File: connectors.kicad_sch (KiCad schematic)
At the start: 13 parts, among them J1 USB-C_JAE_DX07S024JJ2, J2 PCIe_x4_Conn_EdgeMount_Open, J3 Molex_Nano-Fit_1x2_1053131102

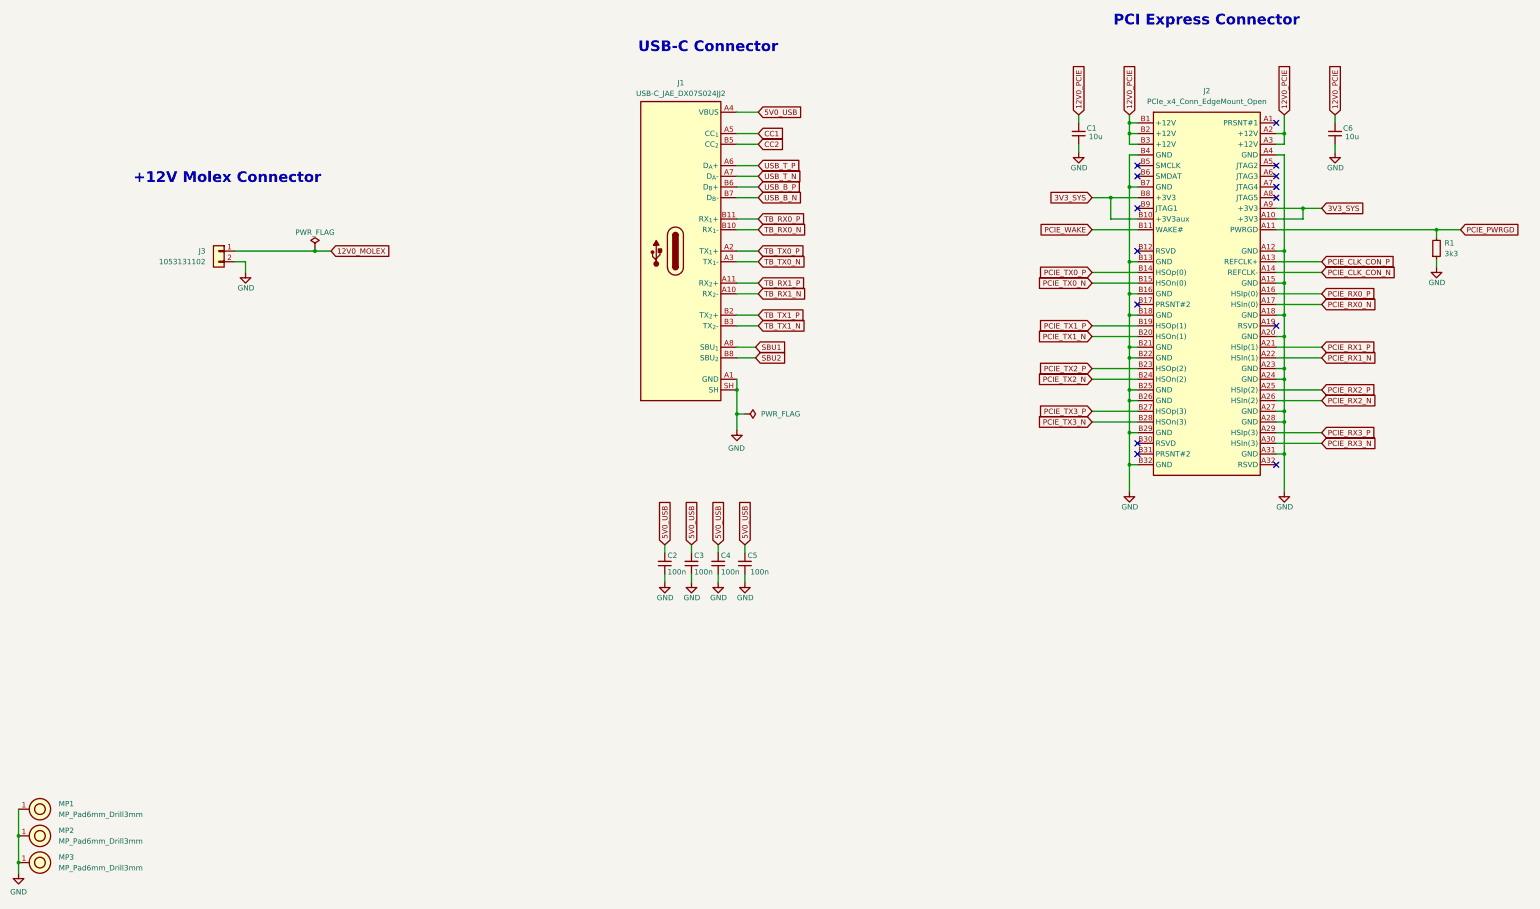
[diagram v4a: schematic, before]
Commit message: [#58582] Update symbols values visibility
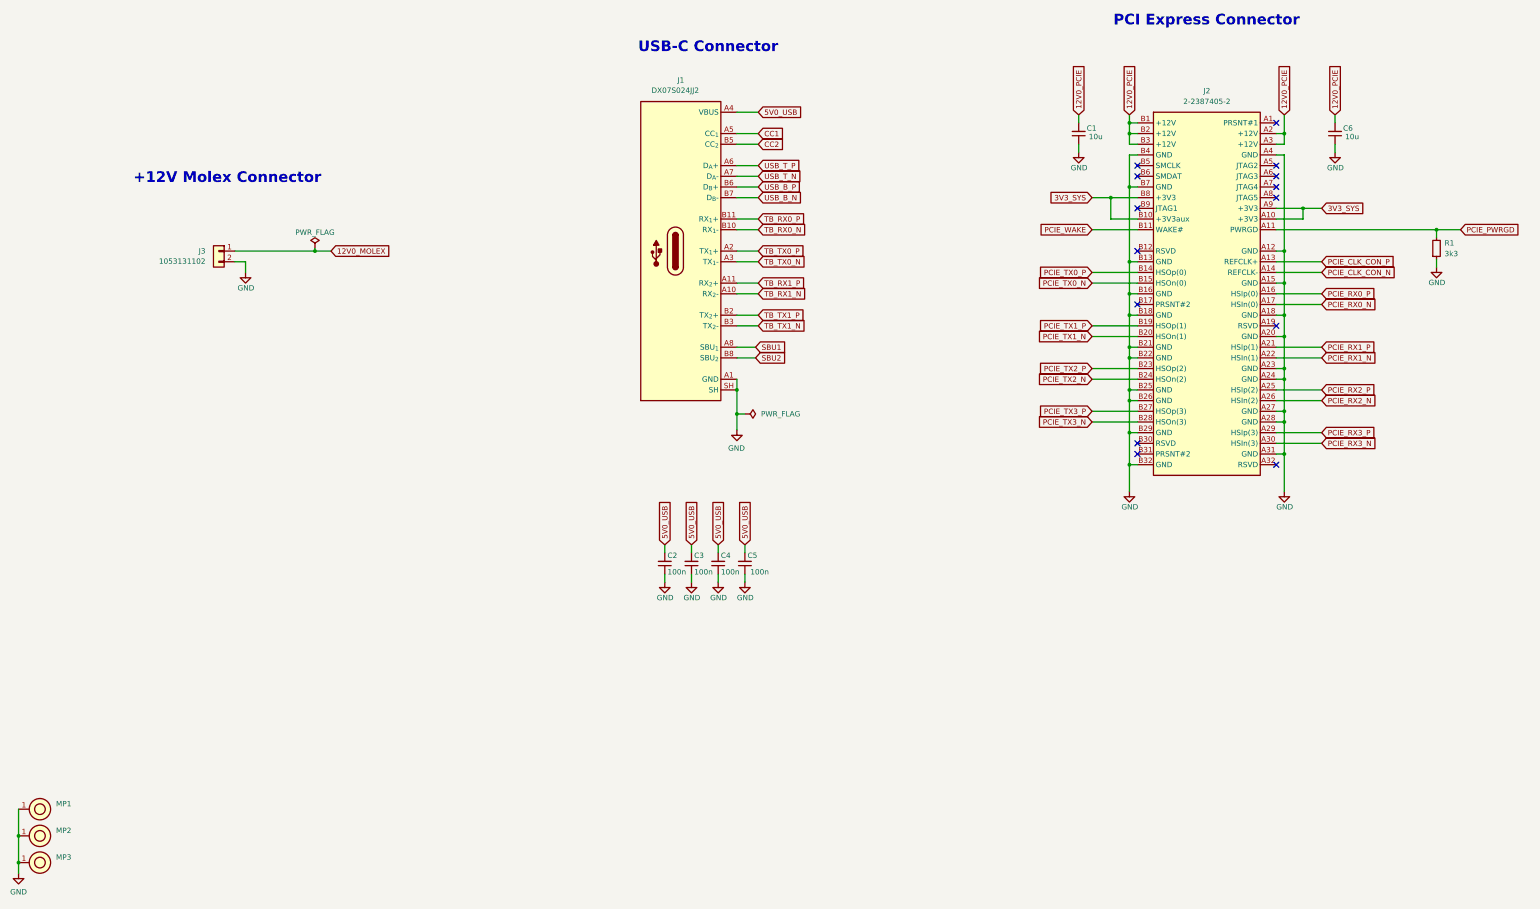
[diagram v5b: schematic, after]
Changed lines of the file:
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@@
   (symbol (lib_id "antmicroMechanicalParts:MP_Pad6mm_Drill3mm") (at 30.48 263.525 0) (unit 1)
     (in_bom no) (on_board yes) (dnp no) (fields_autoplaced)
-    (property "Reference" "MP1" (at 40.005 262.255 0)
+    (property "Reference" "MP1" (at 39.37 262.255 0)
       (effects (font (size 1.27 1.27) (thickness 0.15)) (justify left))
     )
-    (property "Value" "MP_Pad6mm_Drill3mm" (at 40.005 264.795 0)
-      (effects (font (size 1.27 1.27) (thickness 0.15)) (justify left))
+    (property "Value" "MP_Pad6mm_Drill3mm" (at 39.37 264.795 0)
+      (effects (font (size 1.27 1.27) (thickness 0.15)) (justify left) hide)
     )
     (property "Footprint" "antmicro-footprints:MP_Pad6mm_Drill3mm" (at 50.8 271.145 0)
@@
       (effects (font (size 1.27 1.27) (thickness 0.15)) (justify left bottom) hide)
     )
-    (property "MPN" "1053131102" (at 74.93 133.35 0)
-      (effects (font (size 1.27 1.27) (thickness 0.15)) (justify left))
+    (property "MPN" "1053131102" (at 74.93 133.985 0)
+      (effects (font (size 1.27 1.27) (thickness 0.15)) (justify left bottom))
     )
     (property "Author" "Antmicro" (at 68.58 148.59 0)
@@
     )
   )
-  (symbol (lib_name "USB-C_JAE_DX07S024JJ2_1") (lib_id "antmicroUSBConnectors:USB-C_JAE_DX07S024JJ2") (at 201.295 97.79 0) (unit 1)
-    (in_bom yes) (on_board yes) (dnp no) (fields_autoplaced)
-    (property "Reference" "J1" (at 187.96 90.805 0)
+  (symbol (lib_id "antmicroUSBConnectors:USB-C_JAE_DX07S024JJ2") (at 201.295 97.79 0) (unit 1)
+    (in_bom yes) (on_board yes) (dnp no)
+    (property "Reference" "J1" (at 187.96 90.17 0)
       (effects (font (size 1.27 1.27) (thickness 0.15)))
     )
-    (property "Value" "USB-C_JAE_DX07S024JJ2" (at 187.96 93.345 0)
-      (effects (font (size 1.27 1.27) (thickness 0.15)))
+    (property "Value" "USB-C_JAE_DX07S024JJ2" (at 187.96 92.71 0)
+      (effects (font (size 1.27 1.27) (thickness 0.15)) hide)
     )
     (property "Footprint" "antmicro-footprints:USB-C_Receptacle_JAE_DX07S024JJ2" (at 238.125 100.33 0)
@@
       (effects (font (size 1.27 1.27) (thickness 0.15)) (justify left bottom) hide)
     )
-    (property "MPN" "DX07S024JJ2" (at 238.125 105.41 0)
-      (effects (font (size 1.27 1.27) (thickness 0.15)) (justify left bottom) hide)
+    (property "MPN" "DX07S024JJ2" (at 180.975 93.345 0)
+      (effects (font (size 1.27 1.27) (thickness 0.15)) (justify left bottom))
     )
     (property "Manufacturer" "JAE Electronics" (at 238.125 107.95 0)
@@
   (symbol (lib_id "antmicroMechanicalParts:MP_Pad6mm_Drill3mm") (at 30.48 269.875 0) (unit 1)
     (in_bom no) (on_board yes) (dnp no) (fields_autoplaced)
-    (property "Reference" "MP2" (at 40.005 268.605 0)
+    (property "Reference" "MP2" (at 39.37 268.605 0)
       (effects (font (size 1.27 1.27) (thickness 0.15)) (justify left))
     )
-    (property "Value" "MP_Pad6mm_Drill3mm" (at 40.005 271.145 0)
-      (effects (font (size 1.27 1.27) (thickness 0.15)) (justify left))
+    (property "Value" "MP_Pad6mm_Drill3mm" (at 39.37 271.145 0)
+      (effects (font (size 1.27 1.27) (thickness 0.15)) (justify left) hide)
     )
     (property "Footprint" "antmicro-footprints:MP_Pad6mm_Drill3mm" (at 50.8 277.495 0)
@@
       (effects (font (size 1.27 1.27) (thickness 0.15)))
     )
-    (property "Value" "PCIe_x4_Conn_EdgeMount_Open" (at 313.055 95.25 0)
+    (property "Value" "PCIe_x4_Conn_EdgeMount_Open" (at 344.805 105.41 0)
+      (effects (font (size 1.27 1.27) (thickness 0.15)) (justify left bottom) hide)
+    )
+    (property "Footprint" "antmicro-footprints:PCIE_TE_2-2387405-2" (at 344.805 107.95 0)
+      (effects (font (size 1.27 1.27) (thickness 0.15)) (justify left bottom) hide)
+    )
+    (property "Datasheet" "https://www.te.com/commerce/DocumentDelivery/DDEController?Action=showdoc&DocId=Customer+Drawing%7F2387405%7FA%7Fpdf%7FEnglish%7FENG_CD_2387405_A.pdf%7F2-2387405-2" (at 344.805 110.49 0)
+      (effects (font (size 1.27 1.27) (thickness 0.15)) (justify left bottom) hide)
+    )
+    (property "MPN" "2-2387405-2" (at 313.055 95.25 0)
       (effects (font (size 1.27 1.27) (thickness 0.15)))
-    )
-    (property "Footprint" "antmicro-footprints:PCIE_TE_2-2387405-2" (at 344.805 107.95 0)
-      (effects (font (size 1.27 1.27) (thickness 0.15)) (justify left bottom) hide)
-    )
-    (property "Datasheet" "https://www.te.com/commerce/DocumentDelivery/DDEController?Action=showdoc&DocId=Customer+Drawing%7F2387405%7FA%7Fpdf%7FEnglish%7FENG_CD_2387405_A.pdf%7F2-2387405-2" (at 344.805 110.49 0)
-      (effects (font (size 1.27 1.27) (thickness 0.15)) (justify left bottom) hide)
-    )
-    (property "MPN" "2-2387405-2" (at 344.805 113.03 0)
-      (effects (font (size 1.27 1.27) (thickness 0.15)) (justify left bottom) hide)
     )
     (property "Manufacturer" "TE Connectivity" (at 344.805 115.57 0)
@@
   (symbol (lib_id "antmicroMechanicalParts:MP_Pad6mm_Drill3mm") (at 30.48 276.225 0) (unit 1)
     (in_bom no) (on_board yes) (dnp no) (fields_autoplaced)
-    (property "Reference" "MP3" (at 40.005 274.955 0)
+    (property "Reference" "MP3" (at 39.37 274.955 0)
       (effects (font (size 1.27 1.27) (thickness 0.15)) (justify left))
     )
-    (property "Value" "MP_Pad6mm_Drill3mm" (at 40.005 277.495 0)
-      (effects (font (size 1.27 1.27) (thickness 0.15)) (justify left))
+    (property "Value" "MP_Pad6mm_Drill3mm" (at 39.37 277.495 0)
+      (effects (font (size 1.27 1.27) (thickness 0.15)) (justify left) hide)
     )
     (property "Footprint" "antmicro-footprints:MP_Pad6mm_Drill3mm" (at 50.8 283.845 0)

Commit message: [#58582] Update J3, L3 symbols and footprints
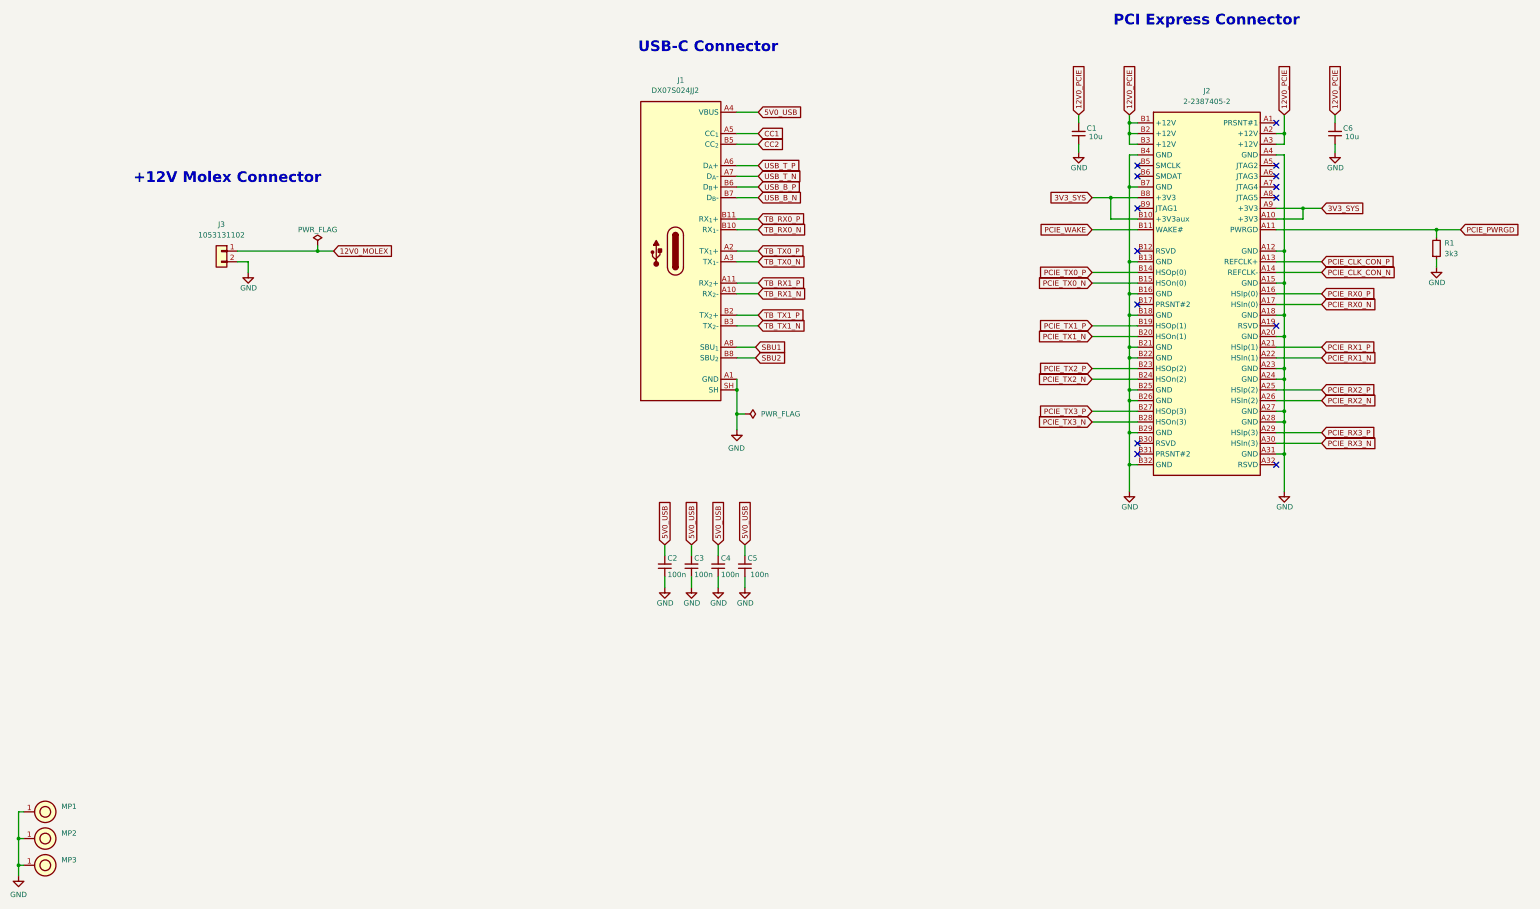
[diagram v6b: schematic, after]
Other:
- moved on the sheet: C2, C3, C4, C5, MP1, MP2, MP3

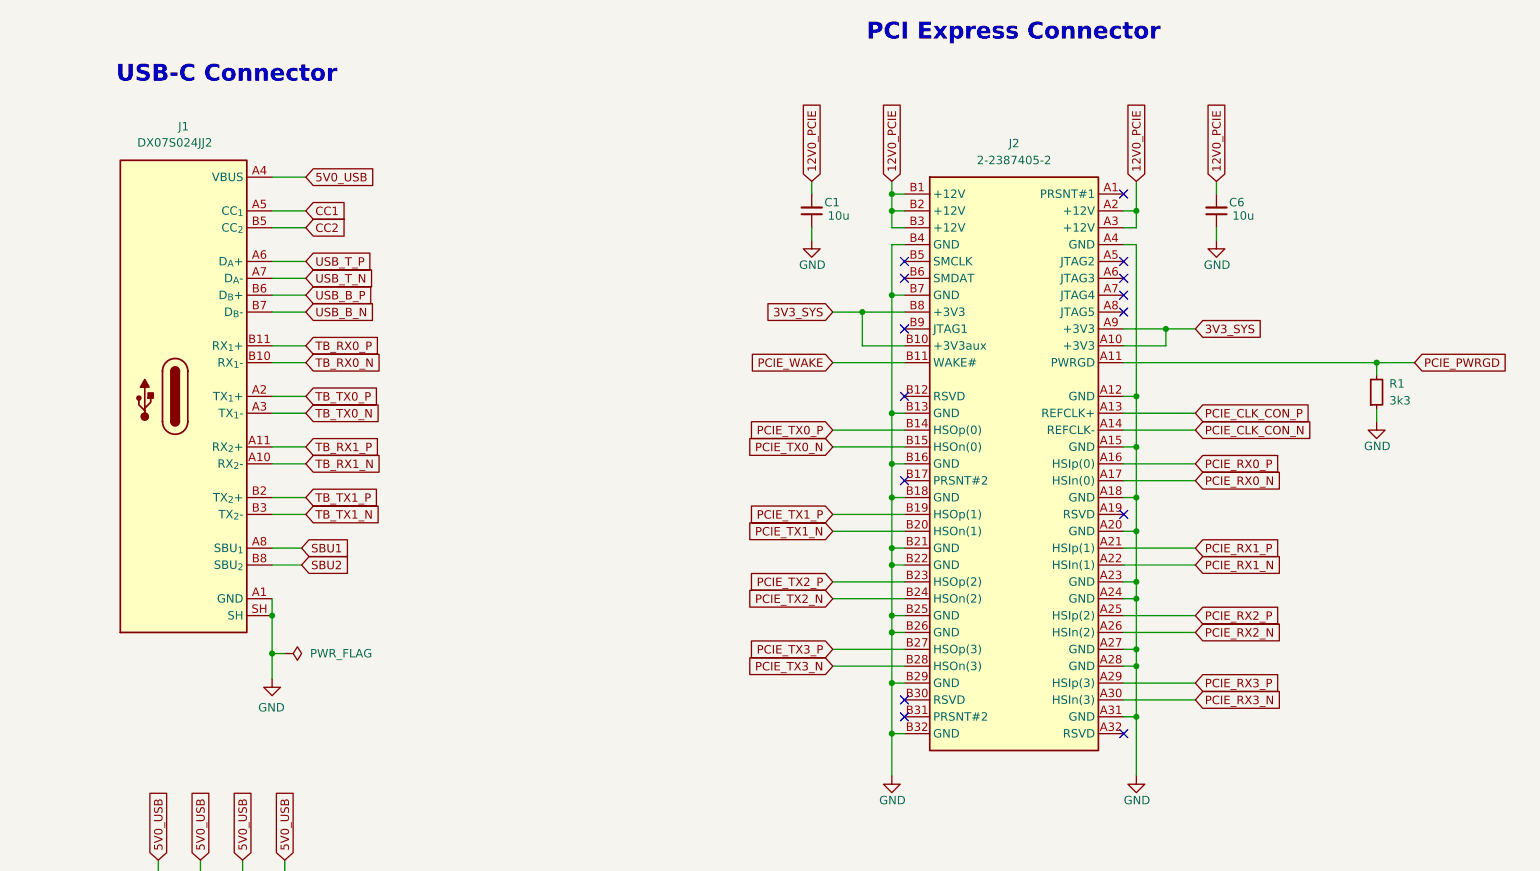
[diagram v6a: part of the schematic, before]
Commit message: [#61922] Update LT8350RV#PBF symbol
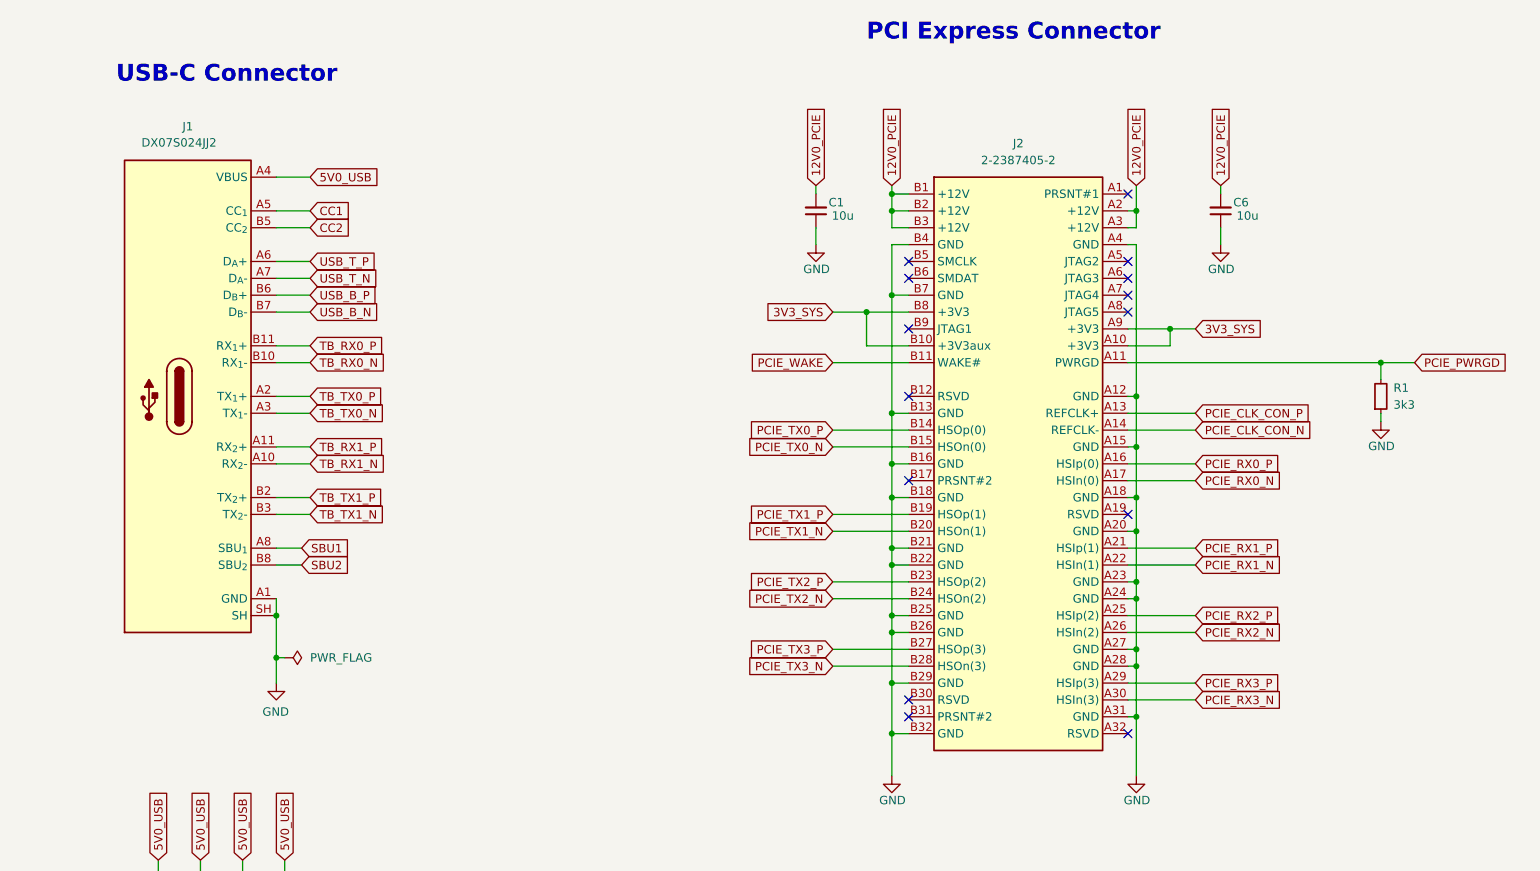
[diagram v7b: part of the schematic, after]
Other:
- moved on the sheet: C1, C6, J1, J2, R1
